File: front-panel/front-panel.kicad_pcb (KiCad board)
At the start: 2 copper layers, 87 x 326.5 mm, 25 parts

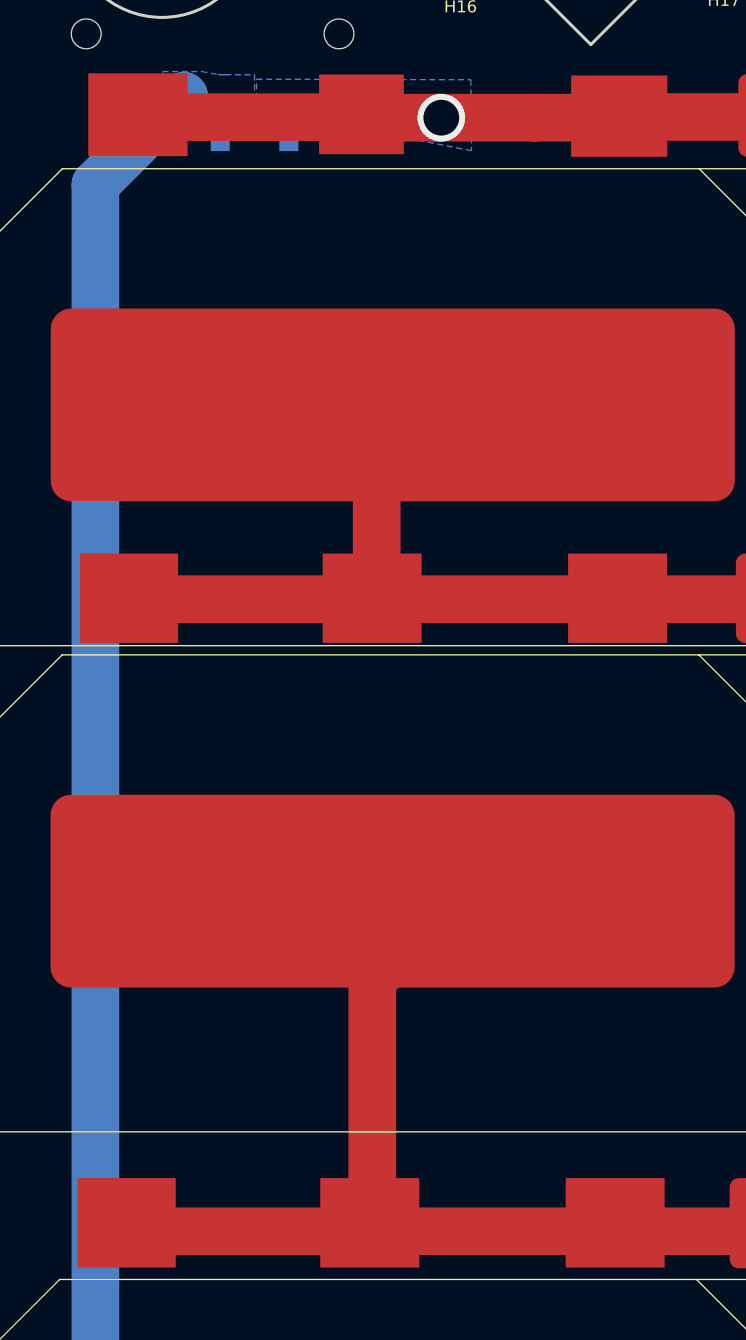
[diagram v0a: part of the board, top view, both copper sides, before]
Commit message: changed cover panels to have smaller power planes, also changed front panel DF13 from SMD to THT
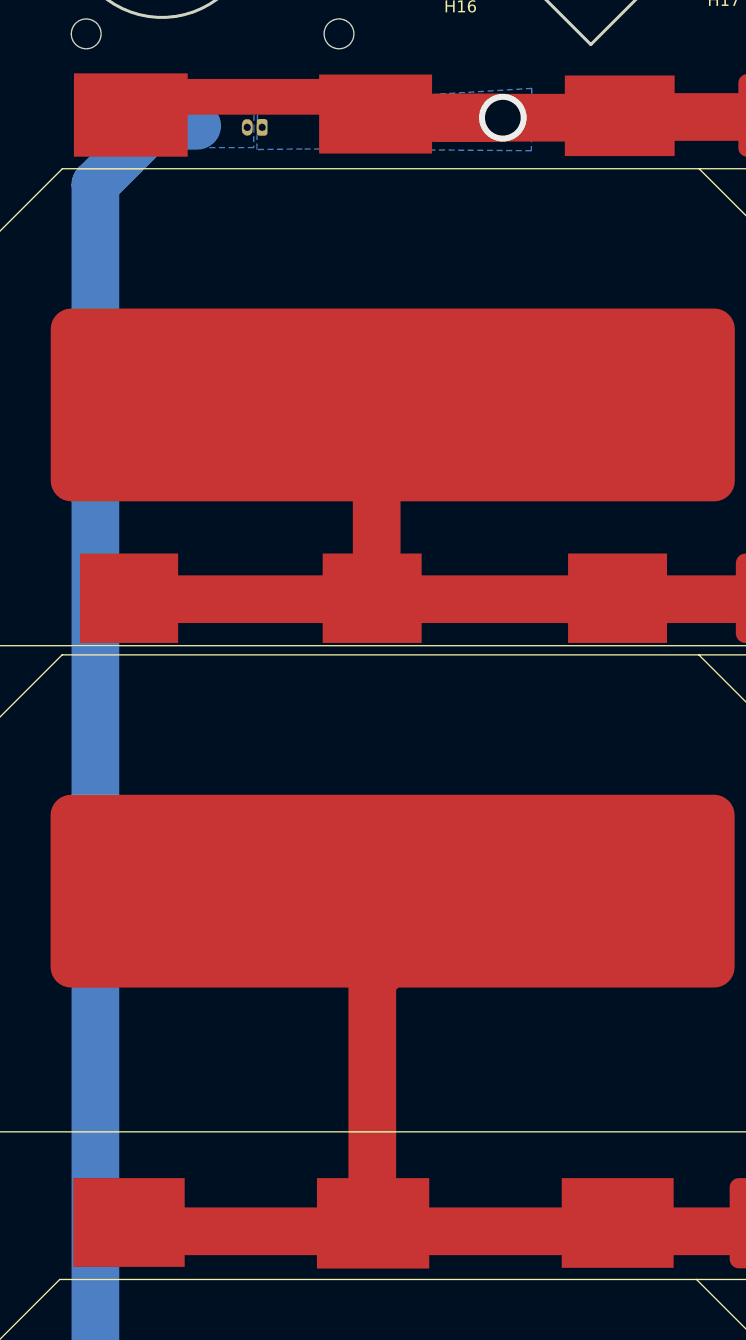
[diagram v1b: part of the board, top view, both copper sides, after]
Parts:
- Buck2: footprint Connection_Pads:2_Hirose_Pin -> Connection_Pads:Hirose_DF13-02P-1.25DSA_1x02_P1.25mm_Vertical
- moved Buck2 10.4 mm to (138.6, 36.8)
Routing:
- net Net-(Buck2-BCR+): track 55.9 -> 68.5 mm
